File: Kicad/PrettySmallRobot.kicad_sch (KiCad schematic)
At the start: 52 parts, among them J1 TYPE-C-31-M-12, J2 S2B-PH-K-S(LF)(SN), J3 S2B-PH-K-S(LF)(SN), J4 S2B-PH-K-S(LF)(SN), SW1 SW_Push, SW2 SW_Push, U1 DRV8837, U2 DRV8837, U3 MCP73831-2ACI_MC, U4 ESP32-S2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

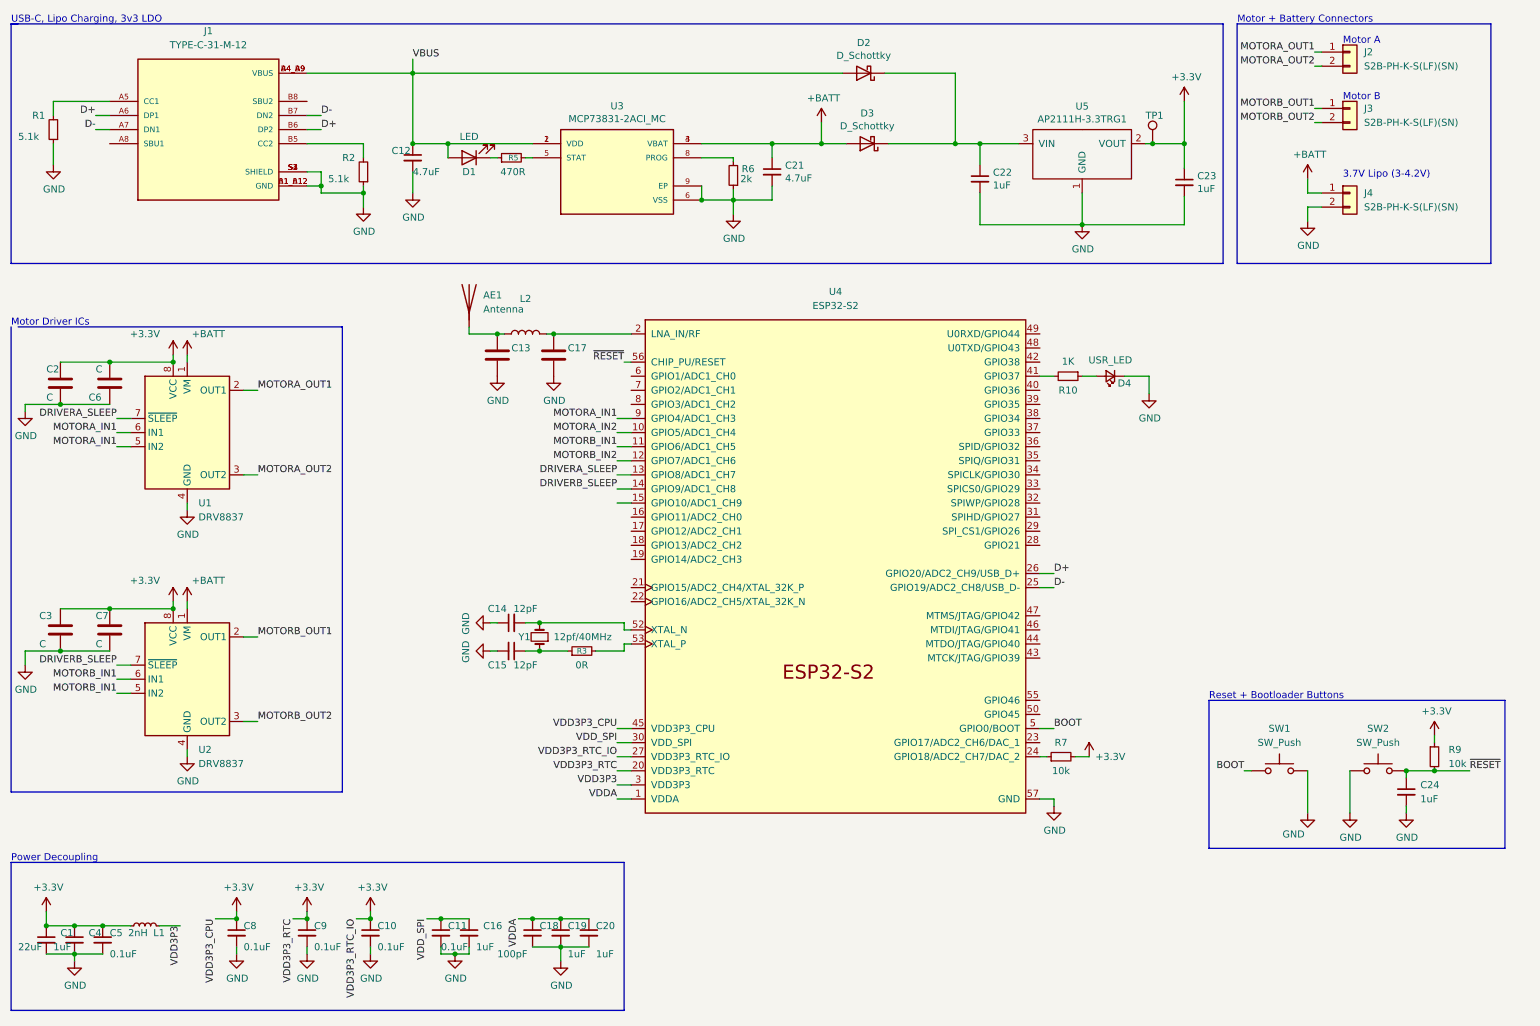
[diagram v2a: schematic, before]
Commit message: matched 90% of parts with footprints
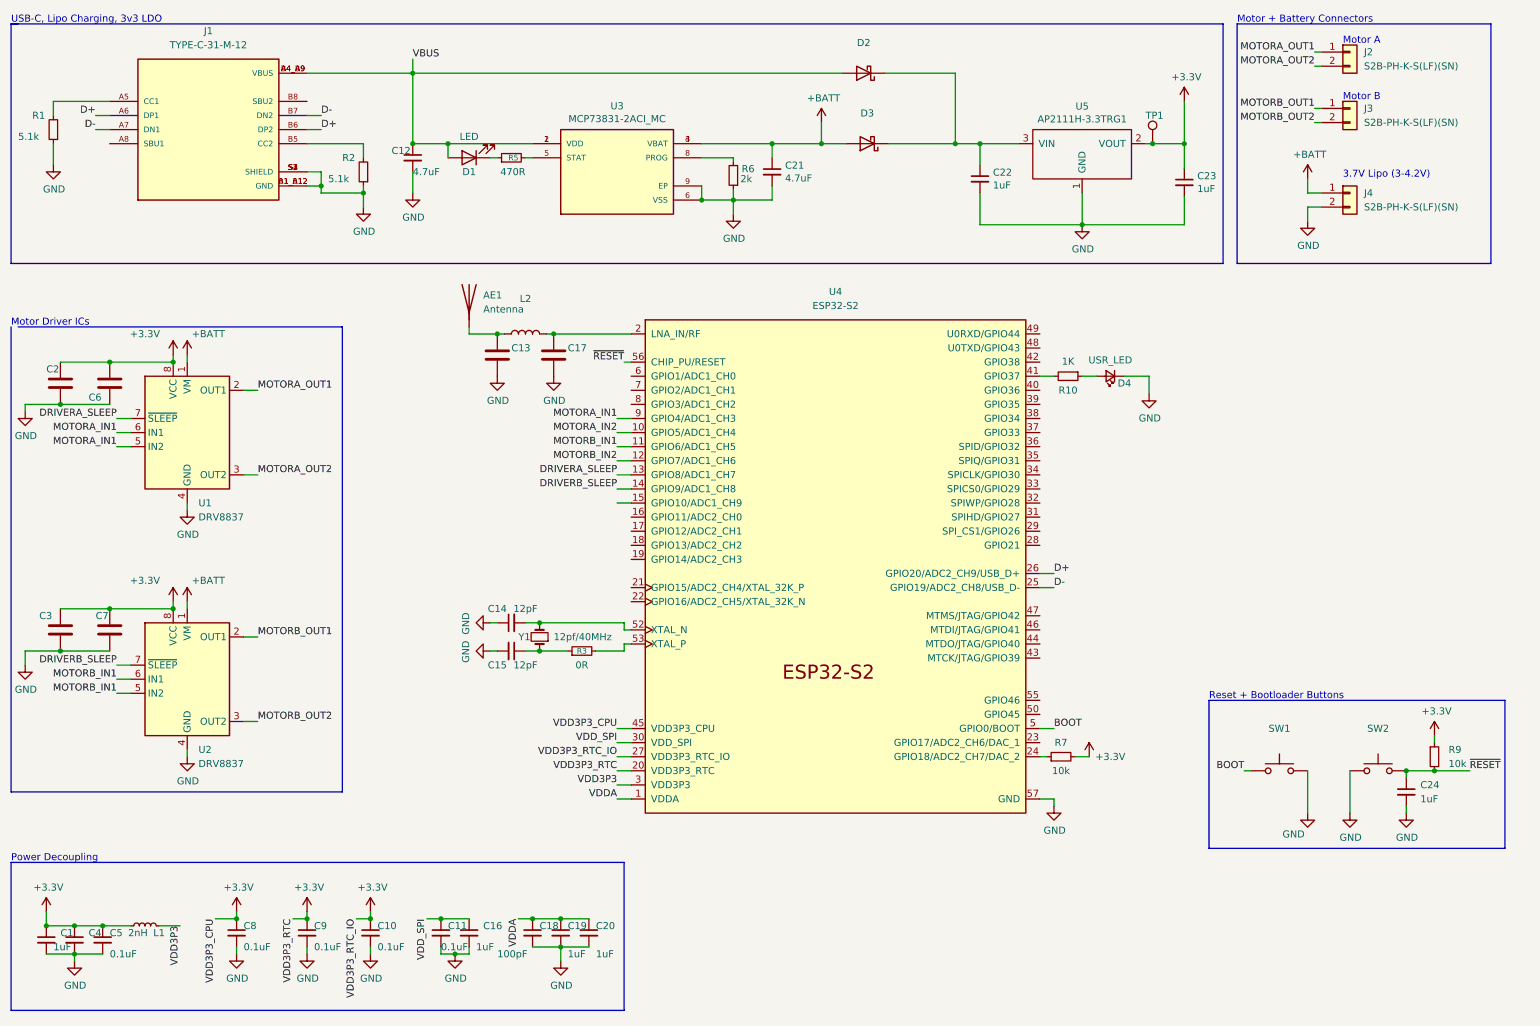
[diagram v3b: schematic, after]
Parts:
- C1: value 22uF -> (none)
- C2, C3, C6, C7: value C -> (none)
- D2, D3: value D_Schottky -> (none); LCSC (none) -> C146335
- SW1, SW2: value SW_Push -> (none); LCSC (none) -> TSA363G25-250B

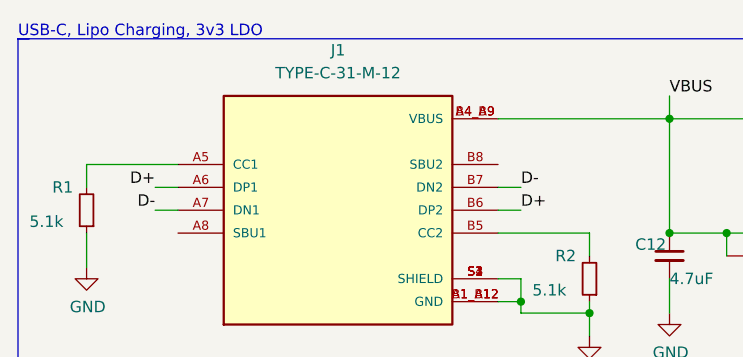
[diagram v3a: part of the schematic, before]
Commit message: preliminary floorplanning done
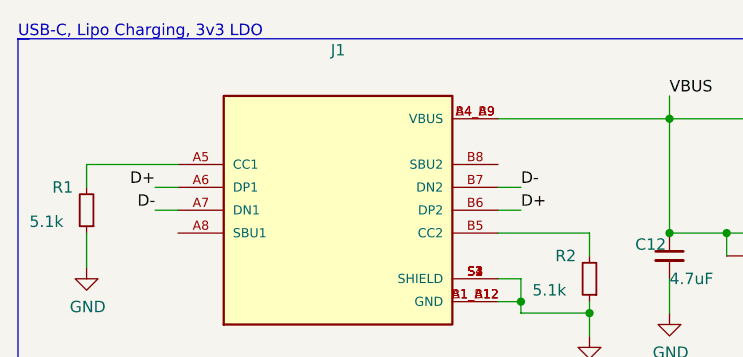
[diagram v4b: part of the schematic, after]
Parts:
- J1: value TYPE-C-31-M-12 -> (none)
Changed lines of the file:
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@@
     (in_bom yes) (on_board yes) (fields_autoplaced)
     (property "Reference" "J1" (id 0) (at 49.53 17.78 0))
-    (property "Value" "TYPE-C-31-M-12" (id 1) (at 49.53 20.32 0))
+    (property "Value" "" (id 1) (at 49.53 20.32 0))
     (property "Footprint" "" (id 2) (at 10.16 29.21 0)
       (effects (font (size 1.27 1.27)) (justify bottom) hide)
@@
     )
     (path "/3c6b0d4e-fccc-417e-bf34-f237c07621e0"
-      (reference "J1") (unit 1) (value "TYPE-C-31-M-12") (footprint "")
+      (reference "J1") (unit 1) (value "TYPE-C-31-M-12") (footprint "kicad_footprints:HRO_TYPE-C-31-M-12")
     )
     (path "/3df40196-e4fa-42be-bb30-c5850f257a4a"
-      (reference "J2") (unit 1) (value "S2B-PH-K-S(LF)(SN)") (footprint "")
+      (reference "J2") (unit 1) (value "S2B-PH-K-S(LF)(SN)") (footprint "Connector_JST:JST_PH_S2B-PH-K_1x02_P2.00mm_Horizontal")
     )
     (path "/8c3a71db-8570-4a26-8abb-7b253c8386f5"
-      (reference "J3") (unit 1) (value "S2B-PH-K-S(LF)(SN)") (footprint "")
+      (reference "J3") (unit 1) (value "S2B-PH-K-S(LF)(SN)") (footprint "Connector_JST:JST_PH_S2B-PH-K_1x02_P2.00mm_Horizontal")
     )
     (path "/6502a99f-049b-4441-92af-fda3c2641b16"
-      (reference "J4") (unit 1) (value "S2B-PH-K-S(LF)(SN)") (footprint "")
+      (reference "J4") (unit 1) (value "S2B-PH-K-S(LF)(SN)") (footprint "Connector_JST:JST_PH_S2B-PH-K_1x02_P2.00mm_Horizontal")
     )
     (path "/705dc02d-e1e2-48cd-b58e-8d1e3dfceb42"
@@
     )
     (path "/c2b6c29a-adcf-4ce5-9e2c-65b7d310e409"
-      (reference "R1") (unit 1) (value "5.1k") (footprint "")
+      (reference "R1") (unit 1) (value "5.1k") (footprint "Resistor_SMD:R_0402_1005Metric")
     )
     (path "/4d1d0761-a5e1-4fb0-adbf-44f9db81663e"
-      (reference "R2") (unit 1) (value "5.1k") (footprint "")
+      (reference "R2") (unit 1) (value "5.1k") (footprint "Resistor_SMD:R_0402_1005Metric")
     )
     (path "/902cfec7-3443-4279-8dd8-065ea8652f37"
@@
     )
     (path "/ec3bc84a-5d87-4c22-9f05-f70570e3810f"
-      (reference "Y1") (unit 1) (value "12pf/40MHz") (footprint "")
-    )
-  )
+      (reference "Y1") (unit 1) (value "12pf/40MHz") (footprint "Crystal:Crystal_SMD_3225-4Pin_3.2x2.5mm")
+    )
+  )

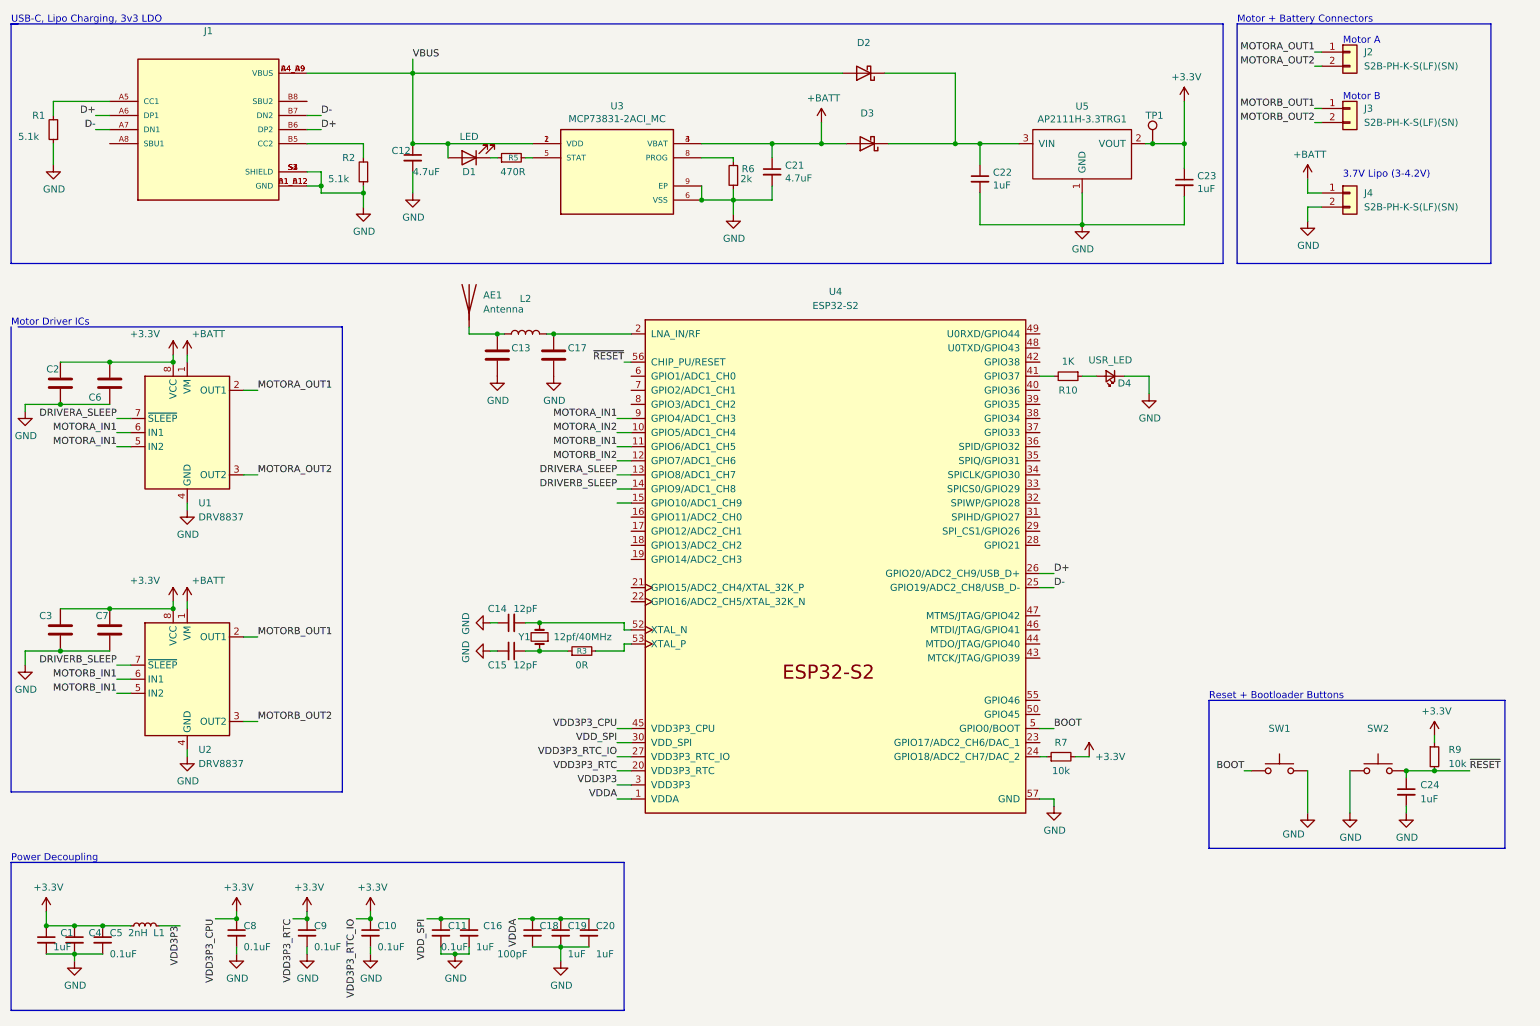
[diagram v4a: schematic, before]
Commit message: replaced 3.3v ldo with ap2112k
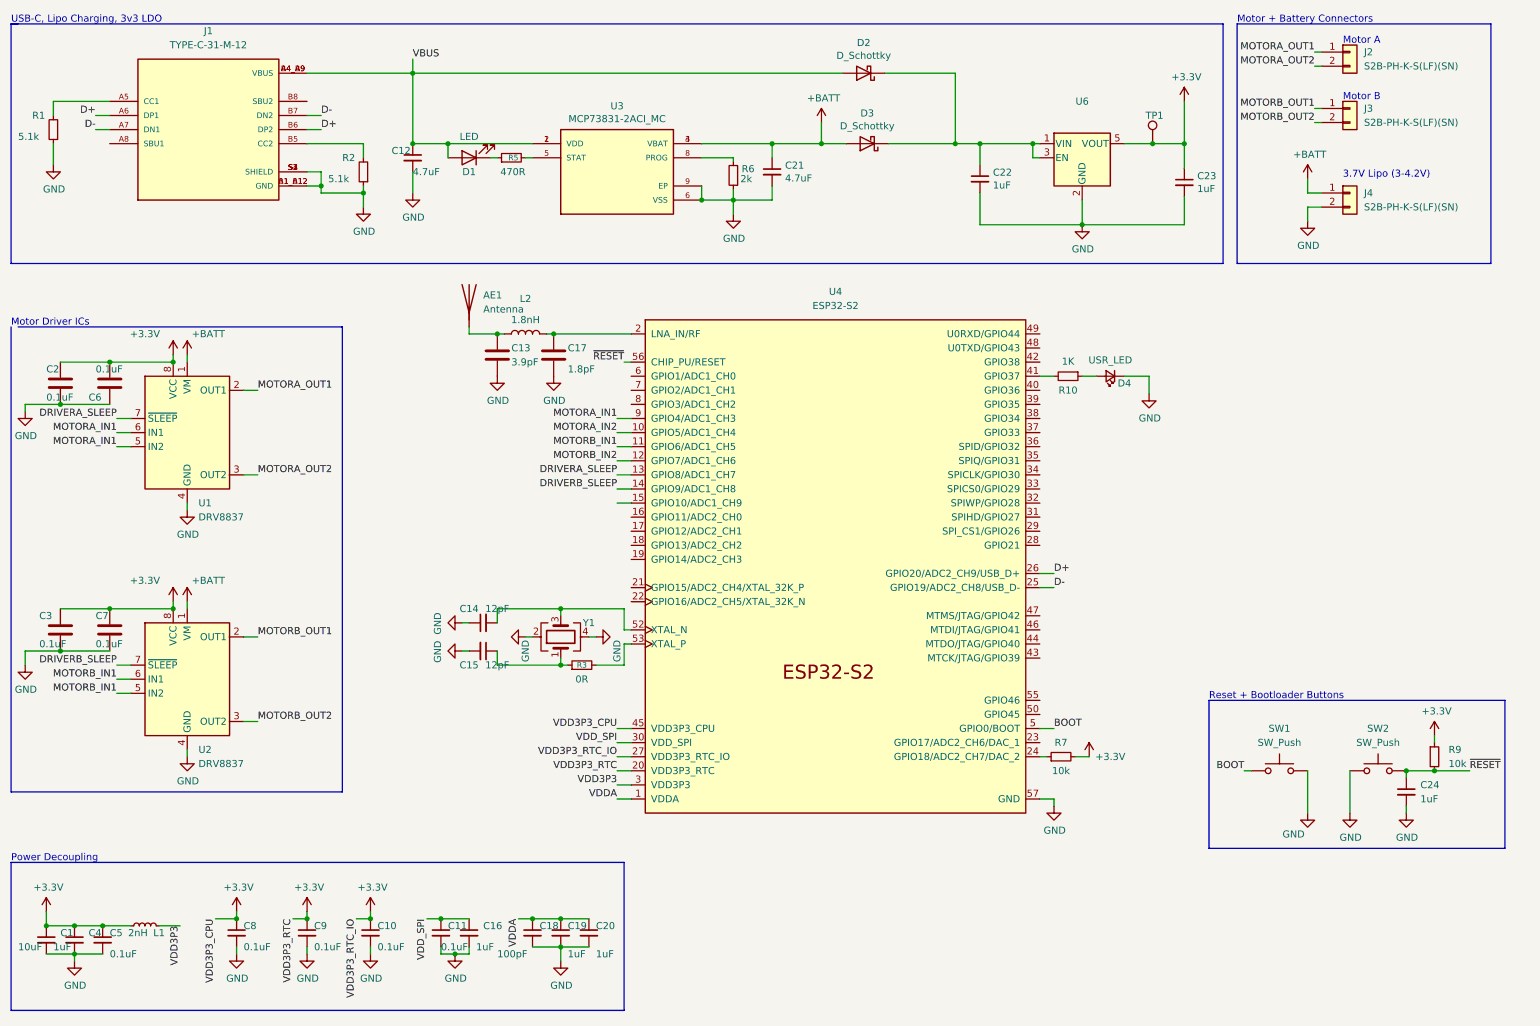
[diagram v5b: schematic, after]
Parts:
- removed U5: AP2111H-3.3TRG1, symbol FSB-rescue:AP2111H-3.3TRG1-Kicad_symbols
- removed Y1: 12pf/40MHz, symbol Device:Crystal_Small
- added U6: (no value), symbol Regulator_Linear:AP2112K-3.3
- added Y1: (no value), symbol Device:Crystal_GND24
- AE1: footprint (none) -> Capacitor_SMD:C_1206_3216Metric
- C1: value (none) -> 10uF; footprint (none) -> Capacitor_SMD:C_0603_1608Metric
- C10, C11, C12, C14, C15, C16, C18, C19, C20, C21, C22, C23, C24, C4, C5, C8, C9: footprint (none) -> Capacitor_SMD:C_0402_1005Metric
- C13: value (none) -> 3.9pF; footprint (none) -> Capacitor_SMD:C_0402_1005Metric
- C17: value (none) -> 1.8pF; footprint (none) -> Capacitor_SMD:C_0402_1005Metric
- C2, C3, C6, C7: value (none) -> 0.1uF; footprint (none) -> Capacitor_SMD:C_0402_1005Metric
- D1, D4: footprint (none) -> LED_SMD:LED_0402_1005Metric
- D2, D3: value (none) -> D_Schottky; footprint (none) -> Diode_SMD:D_SOD-323
- J1: value (none) -> TYPE-C-31-M-12; footprint (none) -> kicad_footprints:HRO_TYPE-C-31-M-12
- J2, J3, J4: footprint (none) -> Connector_JST:JST_PH_S2B-PH-K_1x02_P2.00mm_Horizontal
- L1: footprint (none) -> Inductor_SMD:L_0402_1005Metric
- L2: value (none) -> 1.8nH; footprint (none) -> Inductor_SMD:L_0402_1005Metric
- R1, R10, R2, R3, R5, R6, R7, R9: footprint (none) -> Resistor_SMD:R_0402_1005Metric
- SW1, SW2: value (none) -> SW_Push; footprint (none) -> Button_Switch_SMD:SW_SPST_B3U-1000P
- TP1: footprint (none) -> TestPoint:TestPoint_Plated_Hole_D2.0mm
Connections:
- net +3V3: now also U6.5 (VOUT)
- net GND: now also U6.2 (GND), Y1.2, Y1.4
- net at C22.1, D2.1 (K), D3.1 (K): now also U6.1 (VIN), U6.3 (EN)
- net at C15.1, R3.1: now also Y1.1
- net at C14.2, U4.52 (XTAL_N): now also Y1.3
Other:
- moved on the sheet: C14, C15, R3
